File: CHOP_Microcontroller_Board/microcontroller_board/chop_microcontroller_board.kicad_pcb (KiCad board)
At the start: 4 copper layers, 126.4 x 69.8 mm, 32 parts, among them J11 HEATER_SIGNAL_1, J12 POWER_HEAT, J14 BatteryToMainBoard, J2 OLED, J3 Encoder, J6 PFLOW, J7 DISC PUMP, U1 Teensy4.1_Mounted, U2 U3V50F24, U3 U3V50F12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

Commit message: PCB Final 5/24
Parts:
- added J8: RTC, Connector_PinHeader_2.54mm:PinHeader_1x05_P2.54mm_Vertical, B.Cu at (185.8, 77.5)
- J14: footprint Connector_JST:JST_EH_S2B-EH_1x02_P2.50mm_Horizontal -> Connector_JST:JST_PH_S3B-PH-K_1x03_P2.00mm_Horizontal
- J2, J3: moved to B.Cu
- J6: footprint Connector_PinHeader_2.54mm:PinHeader_1x05_P2.54mm_Vertical -> Connector_Molex:Molex_Micro-Fit_3.0_43650-0500_1x05_P3.00mm_Horizontal
- R6: value 470k -> 4.7k
- R7: value 220k -> 2.2k
- moved J3 15.0 mm to (151.2, 105.0), turned to 180 degrees
- moved U4 7.15 mm to (160.0, 81.0)
- moved J14 5.41 mm to (94.5, 93.5)
- moved J6 4.47 mm to (204.2, 87.3), turned to -90 degrees
- turned J2 to 180 degrees
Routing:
- net /SCL: track 150.8 -> 219.0 mm
- net +3.3V: track 79.2 -> 35.7 mm
- net /ANALOG_FLOW: track 128.5 -> 94.4 mm
- net Net-(J14-Pin_3): track 0.00 -> 31.6 mm
- net /SDA: track 159.6 -> 182.1 mm
- net ENC_B: track 29.4 -> 49.1 mm
- net ENC_A: track 35.6 -> 42.0 mm
- net ENC_SW: track 43.5 -> 39.2 mm

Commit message: PCB update 5/27
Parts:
- moved J12 72.3 mm to (204.5, 90.0), turned to -90 degrees
- moved J6 38.2 mm to (166.7, 80.3), turned to 0 degrees
- moved U4 3.92 mm to (160.0, 84.9)
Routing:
- net /ANALOG_FLOW: track 94.4 -> 70.9 mm
- net +5V: track 12.0 -> 23.5 mm
- net /SCL: track 219.0 -> 230.0 mm
- net /SDA: track 182.1 -> 186.4 mm

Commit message: CHOP 3d models 5/30
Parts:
- J14: footprint Connector_JST:JST_PH_S3B-PH-K_1x03_P2.00mm_Horizontal -> Connector_JST:JST_PH_S2B-PH-K_1x02_P2.00mm_Horizontal
- J2: footprint Connector_PinHeader_2.54mm:PinHeader_1x04_P2.54mm_Vertical -> chop_footprint_library:128x64OLED
- moved J2 28.5 mm to (180.0, 108.0), turned to 90 degrees
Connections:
- U1 pad 17: Net-(J14-Pin_3) -> unconnected-(U1-25_A11_RX6_SDA2-Pad17)
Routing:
- net Net-(J14-Pin_3): track 31.6 -> 0.00 mm
- net /SDA: track 186.4 -> 166.7 mm
- net /SCL: track 230.0 -> 215.4 mm

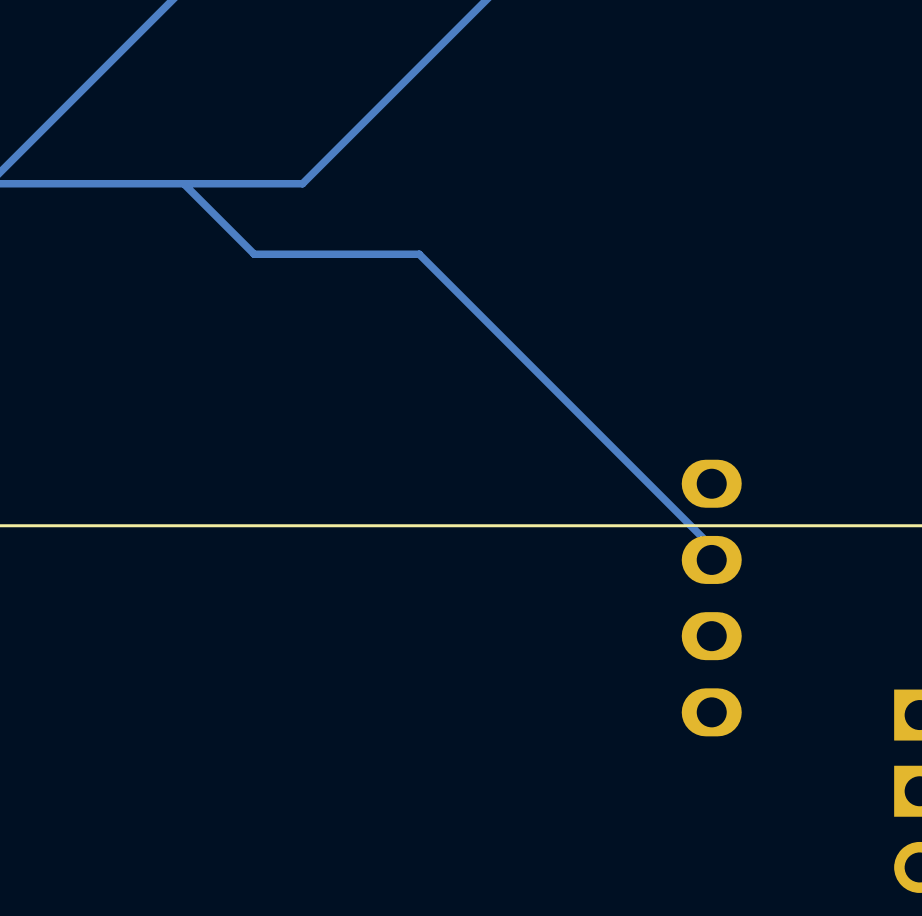
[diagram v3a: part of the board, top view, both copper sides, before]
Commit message: CHOP MCU update OLED
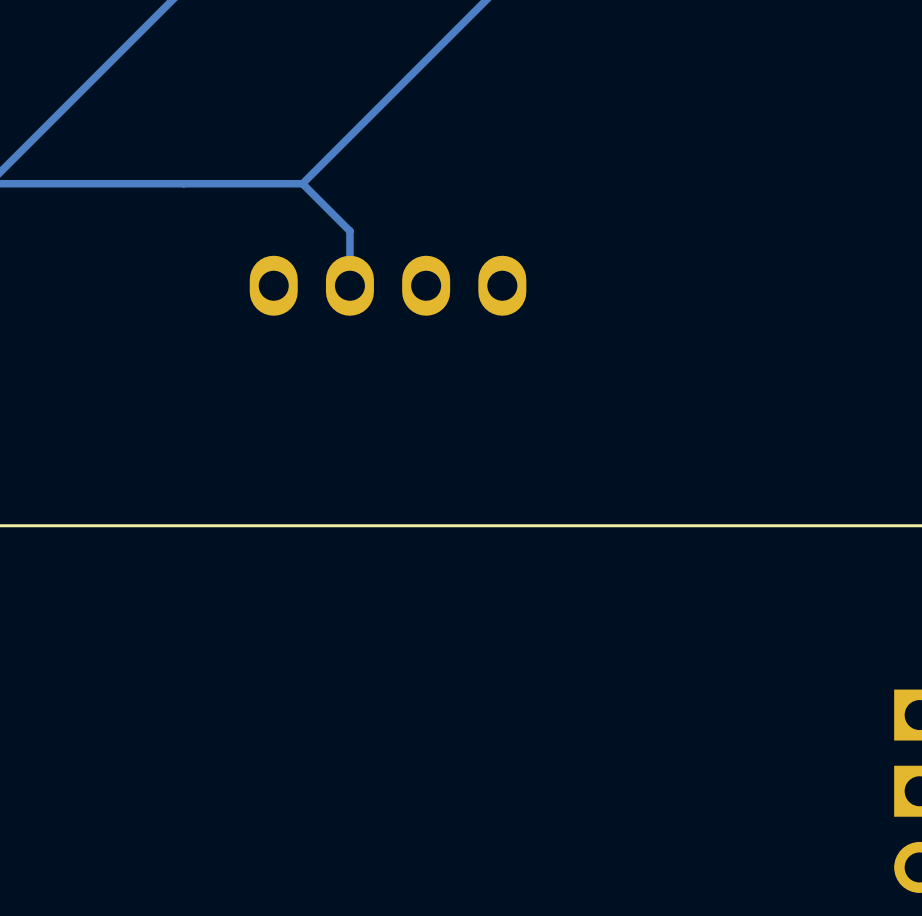
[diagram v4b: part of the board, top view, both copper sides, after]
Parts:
- turned J2 to 180 degrees
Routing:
- net /SCL: track 215.4 -> 160.0 mm
- net /SDA: track 166.7 -> 147.7 mm
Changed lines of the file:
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@@
 	(footprint "chop_footprint_library:128x64OLED"
 		(layer "B.Cu")
-		(at 180 108 90)
+		(at 180 108 180)
 		(property "Reference" "J2"
-			(at 1.92 -0.254 90)
+			(at 1.92 -0.254 0)
 			(layer "B.SilkS")
 			(effects
@@
 		)
 		(property "Value" "OLED"
-			(at 7.62 7.62 90)
+			(at 7.62 7.62 0)
 			(layer "B.Fab")
 			(effects
@@
 		)
 		(property "Datasheet" ""
-			(at 0 0 90)
+			(at 0 0 0)
 			(layer "B.Fab")
 			(hide yes)
@@
 		)
 		(property "Description" "Generic connector, single row, 01x04, script generated (kicad-library-utils/schlib/autogen/connector/)"
-			(at 0 0 90)
+			(at 0 0 0)
 			(layer "B.Fab")
 			(hide yes)
@@
 		(attr through_hole)
 		(fp_line
+			(start 14 12.3)
+			(end 14 -15)
+			(stroke
+				(width 0.12)
+				(type solid)
+			)
+			(layer "B.SilkS")
+		)
+		(fp_line
 			(start 14 -15)
 			(end -13.4 -15)
@@
 		)
 		(fp_line
+			(start 13.462 9.017)
+			(end 13.208 9.005)
+			(stroke
+				(width 0.12)
+				(type solid)
+			)
+			(layer "B.SilkS")
+		)
+		(fp_line
+			(start 13.462 -7.62)
+			(end 13.462 9.017)
+			(stroke
+				(width 0.12)
+				(type solid)
+			)
+			(layer "B.SilkS")
+		)
+		(fp_line
+			(start 10.122 9.005)
+			(end 13.208 9.005)
+			(stroke
+				(width 0.12)
+				(type solid)
+			)
+			(layer "B.SilkS")
+		)
+		(fp_line
+			(start 10.122 -7.595)
+			(end 13.462 -7.62)
+			(stroke
+				(width 0.12)
+				(type solid)
+			)
+			(layer "B.SilkS")
+		)
+		(fp_line
+			(start 10.122 -7.595)
+			(end -12.978 -7.595)
+			(stroke
+				(width 0.12)
+				(type solid)
+			)
+			(layer "B.SilkS")
+		)
+		(fp_line
+			(start 5.08 11.811)
+			(end 5.08 9.398)
+			(stroke
+				(width 0.12)
+				(type solid)
+			)
+			(layer "B.SilkS")
+		)
+		(fp_line
+			(start 5.08 9.398)
+			(end -4.699 9.398)
+			(stroke
+				(width 0.12)
+				(type solid)
+			)
+			(layer "B.SilkS")
+		)
+		(fp_line
+			(start -4.699 11.811)
+			(end 5.08 11.811)
+			(stroke
+				(width 0.12)
+				(type solid)
+			)
+			(layer "B.SilkS")
+		)
+		(fp_line
+			(start -4.699 11.811)
+			(end -4.699 9.398)
+			(stroke
+				(width 0.12)
+				(type solid)
+			)
+			(layer "B.SilkS")
+		)
+		(fp_line
+			(start -12.978 9.005)
+			(end 10.122 9.005)
+			(stroke
+				(width 0.12)
+				(type solid)
+			)
+			(layer "B.SilkS")
+		)
+		(fp_line
+			(start -12.978 -7.595)
+			(end -12.978 9.005)
+			(stroke
+				(width 0.12)
+				(type solid)
+			)
+			(layer "B.SilkS")
+		)
+		(fp_line
+			(start -13.4 12.3)
+			(end 14 12.3)
+			(stroke
+				(width 0.12)
+				(type solid)
+			)
+			(layer "B.SilkS")
+		)
+		(fp_line
 			(start -13.4 -15)
 			(end -13.4 12.3)
@@
 			(layer "B.SilkS")
 		)
-		(fp_line
-			(start 13.462 -7.62)
-			(end 13.462 9.017)
-			(stroke
-				(width 0.12)
-				(type solid)
-			)
-			(layer "B.SilkS")
-		)
-		(fp_line
-			(start 10.122 -7.595)
-			(end 13.462 -7.62)
-			(stroke
-				(width 0.12)
-				(type solid)
-			)
-			(layer "B.SilkS")
-		)
-		(fp_line
-			(start 10.122 -7.595)
-			(end -12.978 -7.595)
-			(stroke
-				(width 0.12)
-				(type solid)
-			)
-			(layer "B.SilkS")
-		)
-		(fp_line
-			(start -12.978 -7.595)
-			(end -12.978 9.005)
-			(stroke
-				(width 0.12)
-				(type solid)
-			)
-			(layer "B.SilkS")
-		)
-		(fp_line
-			(start 10.122 9.005)
-			(end 13.208 9.005)
-			(stroke
-				(width 0.12)
-				(type solid)
-			)
-			(layer "B.SilkS")
-		)
-		(fp_line
-			(start -12.978 9.005)
-			(end 10.122 9.005)
-			(stroke
-				(width 0.12)
-				(type solid)
-			)
-			(layer "B.SilkS")
-		)
-		(fp_line
-			(start 13.462 9.017)
-			(end 13.208 9.005)
-			(stroke
-				(width 0.12)
-				(type solid)
-			)
-			(layer "B.SilkS")
-		)
-		(fp_line
-			(start 5.08 9.398)
-			(end -4.699 9.398)
-			(stroke
-				(width 0.12)
-				(type solid)
-			)
-			(layer "B.SilkS")
-		)
-		(fp_line
-			(start 5.08 11.811)
-			(end 5.08 9.398)
-			(stroke
-				(width 0.12)
-				(type solid)
-			)
-			(layer "B.SilkS")
-		)
-		(fp_line
-			(start -4.699 11.811)
-			(end -4.699 9.398)
-			(stroke
-				(width 0.12)
-				(type solid)
-			)
-			(layer "B.SilkS")
-		)
-		(fp_line
-			(start -4.699 11.811)
-			(end 5.08 11.811)
-			(stroke
-				(width 0.12)
-				(type solid)
-			)
-			(layer "B.SilkS")
-		)
-		(fp_line
-			(start 14 12.3)
-			(end 14 -15)
-			(stroke
-				(width 0.12)
-				(type solid)
-			)
-			(layer "B.SilkS")
-		)
-		(fp_line
-			(start -13.4 12.3)
-			(end 14 12.3)
-			(stroke
-				(width 0.12)
-				(type solid)
-			)
-			(layer "B.SilkS")
-		)
 		(fp_text user "${REFERENCE}"
-			(at 0 -3.81 0)
+			(at 0 -3.81 90)
 			(layer "B.Fab")
 			(effects
@@
 		)
 		(pad "1" thru_hole oval
-			(at -3.62 10.6)
+			(at -3.62 10.6 90)
 			(size 2 1.6)
 			(drill 1)
@@
 		)
 		(pad "2" thru_hole oval
-			(at -1.08 10.6)
+			(at -1.08 10.6 90)
 			(size 2 1.6)
 			(drill 1)
@@
 		)
 		(pad "3" thru_hole oval
-			(at 1.46 10.6)
+			(at 1.46 10.6 90)
 			(size 2 1.6)
 			(drill 1)
@@
 		)
 		(pad "4" thru_hole oval
-			(at 4 10.6)
+			(at 4 10.6 90)
 			(size 2 1.6)
 			(drill 1)
@@
 	)
 	(segment
-		(start 212.5 86.5)
-		(end 212.5 102.42)
-		(width 0.25)
-		(layer "In1.Cu")
-		(net 12)
-	)
-	(segment
 		(start 145.5 92.5)
 		(end 140.973116 92.5)
@@
 	)
 	(segment
-		(start 168 97.81)
-		(end 174.19 104)
-		(width 0.25)
-		(layer "In1.Cu")
-		(net 12)
-	)
-	(segment
 		(start 150.81 97.81)
 		(end 145.5 92.5)
@@
 	)
 	(segment
-		(start 212.5 102.42)
-		(end 210.92 104)
-		(width 0.25)
-		(layer "In1.Cu")
-		(net 12)
-	)
-	(segment
-		(start 210 84)
-		(end 212.5 86.5)
-		(width 0.25)
-		(layer "In1.Cu")
-		(net 12)
-	)
-	(segment
-		(start 174.19 104)
-		(end 190.6 104)
+		(start 168 97.81)
+		(end 175.59 97.81)
+		(width 0.25)
+		(layer "In1.Cu")
+		(net 12)
+	)
+	(segment
+		(start 175.59 97.81)
+		(end 176 97.4)
 		(width 0.25)
 		(layer "In1.Cu")
@@
 	)
 	(segment
-		(start 210.92 104)
-		(end 190.6 104)
-		(width 0.25)
-		(layer "In1.Cu")
-		(net 12)
-	)
-	(segment
 		(start 190.92 77.5)
 		(end 192 78.58)
@@
 	)
 	(segment
+		(start 176.6 97.4)
+		(end 192 82)
+		(width 0.25)
+		(layer "In1.Cu")
+		(net 12)
+	)
+	(segment
 		(start 192 78.58)
 		(end 192 82)
@@
 	)
 	(segment
-		(start 192 82)
-		(end 194 84)
-		(width 0.25)
-		(layer "In1.Cu")
-		(net 12)
-	)
-	(segment
-		(start 194 84)
-		(end 210 84)
+		(start 176 97.4)
+		(end 176.6 97.4)
 		(width 0.25)
 		(layer "In1.Cu")
@@
 	)
 	(segment
+		(start 178.54 97.4)
+		(end 178.54 95.58)
+		(width 0.25)
+		(layer "B.Cu")
+		(net 14)
+	)
+	(segment
 		(start 176.96 94)
 		(end 173 94)
@@
 	)
 	(segment
-		(start 190.6 106.54)
-		(end 190.6 106.1)
+		(start 178.54 95.58)
+		(end 176.96 94)
 		(width 0.25)
 		(layer "B.Cu")
@@
 	(segment
 		(start 173 94)
-		(end 175.35 96.35)
-		(width 0.25)
-		(layer "B.Cu")
-		(net 14)
-	)
-	(segment
-		(start 173 94)
 		(end 166.5 94)
-		(width 0.25)
-		(layer "B.Cu")
-		(net 14)
-	)
-	(segment
-		(start 175.35 96.35)
-		(end 180.85 96.35)
 		(width 0.25)
 		(layer "B.Cu")
@@
 		(width 0.25)
 		(layer "B.Cu")
-		(net 14)
-	)
-	(segment
-		(start 190.6 106.1)
-		(end 180.85 96.35)
-		(width 0.25)
-		(layer "B.Cu")
